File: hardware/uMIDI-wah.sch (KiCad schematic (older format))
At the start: 33 parts, among them IC1 Opamp_Dual_Generic, IC2 L78L09_SOT89, SW1 MMP221, X1 AudioJack3_Switch, X3 AudioJack3_Switch, X4 Conn_01x10

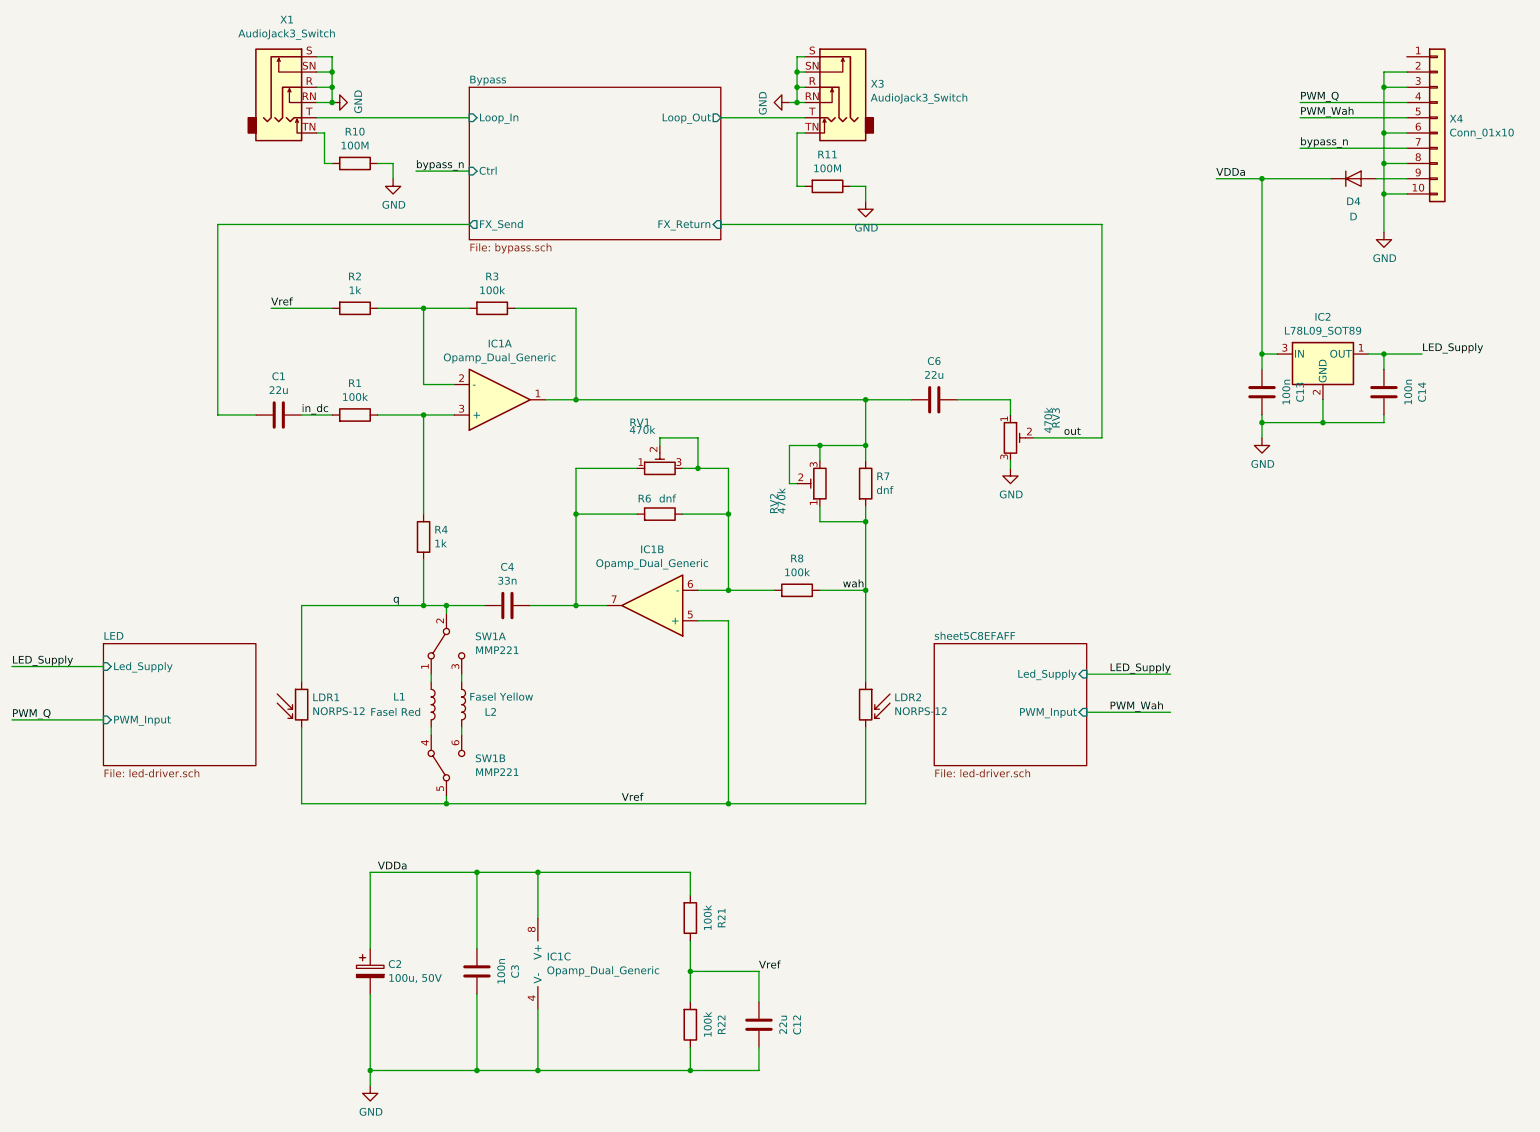
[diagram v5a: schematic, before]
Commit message: Use second relay to switch between inductors
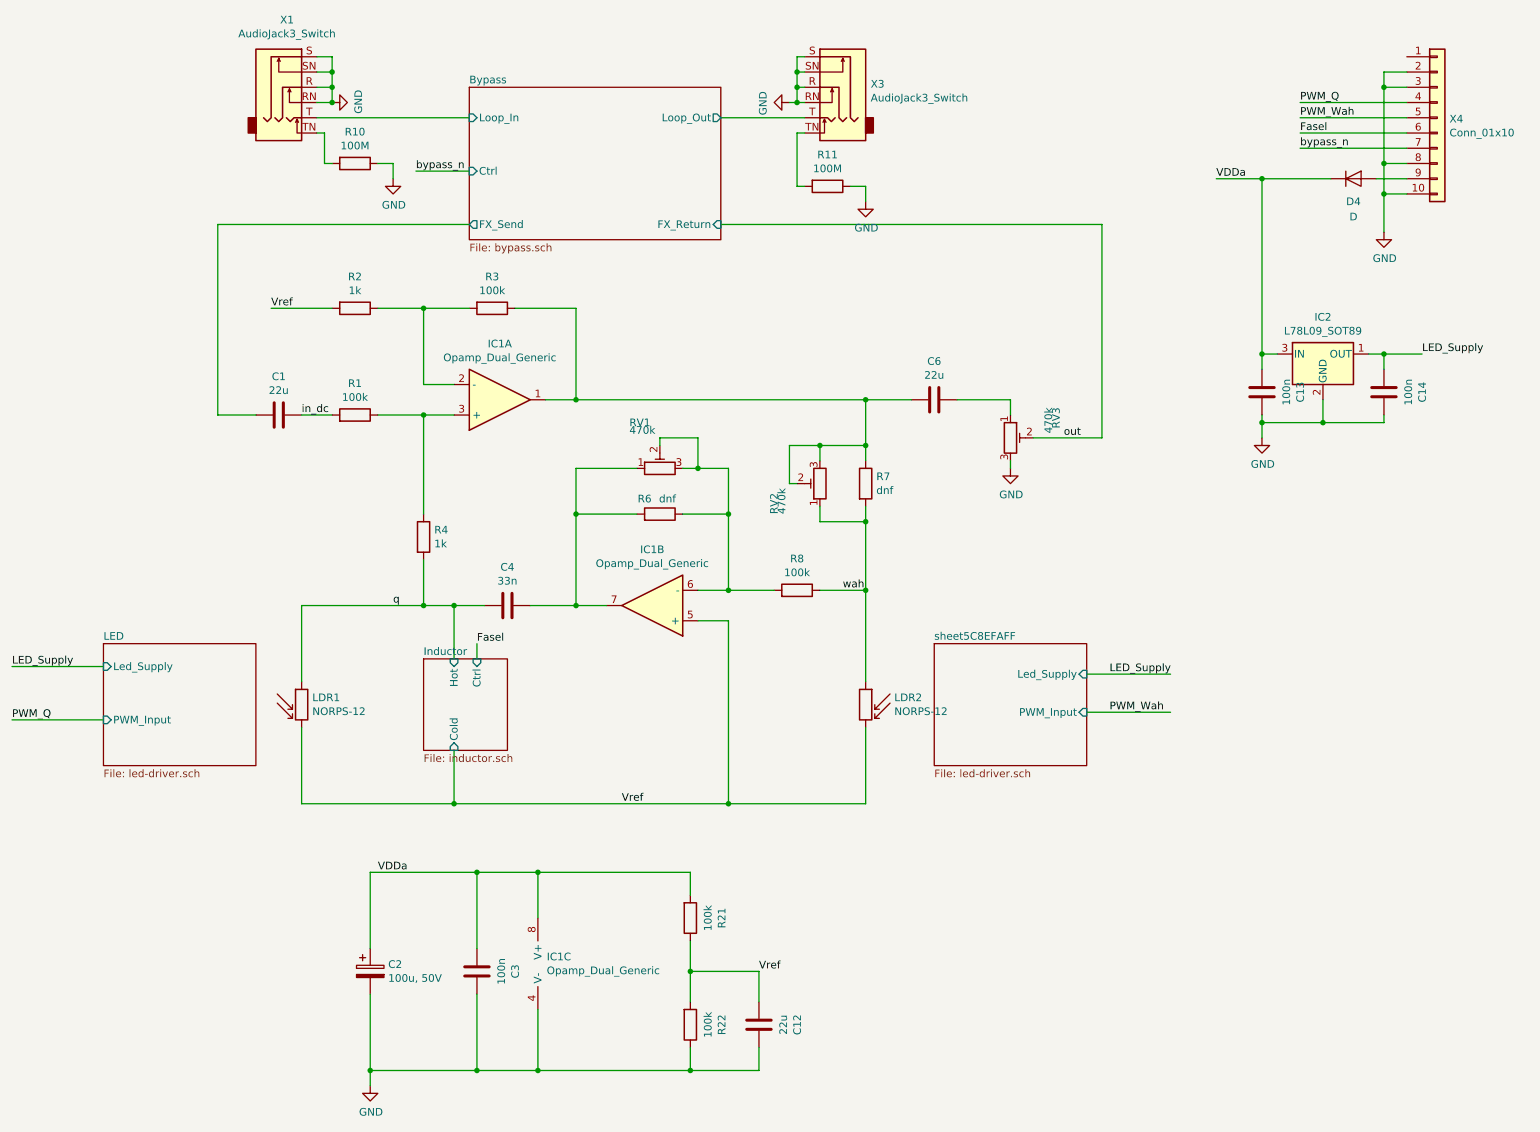
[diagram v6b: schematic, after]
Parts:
- removed L1: Fasel Red, umidi-wah:Fasel, symbol Device:L
- removed L2: Fasel Yellow, umidi-wah:Fasel, symbol Device:L
- removed SW1: MMP221, umidi-wah:MMP221, symbol Switch:SW_DPDT_x2
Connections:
- net GND: no longer X4.6 (Pin_6)
- new net Fasel: X4.6 (Pin_6)
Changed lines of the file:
@@
 $Descr A4 11693 8268
 encoding utf-8
-Sheet 1 4
+Sheet 1 5
 Title ""
 Date ""
@@
 	1    0    0    -1
 $EndComp
-$Comp
-L Device:L L1
-U 1 1 5C88342E
-P 3750 5000
-F 0 "L1" H 3500 5050 50  0000 L CNN
-F 1 "Fasel Red" H 3350 4950 50  0000 L CNN
-F 2 "umidi-wah:Fasel" H 3750 5000 50  0001 C CNN
-F 3 "~" H 3750 5000 50  0001 C CNN
-	1    3750 5000
-	1    0    0    -1
-$EndComp
 Wire Wire Line
 	5700 4250 5700 3750
@@
 Wire Wire Line
 	3700 4050 3700 4350
-Wire Wire Line
-	3700 4350 3850 4350
 Connection ~ 3700 4350
 Wire Wire Line
@@
 	10000 1900 10000 1650
 Wire Wire Line
-	10000 1250 10150 1250
-Wire Wire Line
 	10150 1650 10000 1650
 Connection ~ 10000 1650
@@
 Wire Wire Line
 	10150 1450 10000 1450
-Connection ~ 10000 1450
-Wire Wire Line
-	10000 1450 10000 1250
 Text Label 9450 1350 0    50   ~ 0
 bypass_n
@@
 	1    0    0    -1
 $EndComp
-$Comp
-L Switch:SW_DPDT_x2 SW1
-U 2 1 5CDB9DAE
-P 3850 5400
-F 0 "SW1" V 3896 5212 50  0000 R CNN
-F 1 "MMP221" V 3805 5212 50  0000 R CNN
-F 2 "umidi-wah:MMP221" H 3850 5400 50  0001 C CNN
-F 3 "https://docs-emea.rs-online.com/webdocs/0e2b/0900766b80e2b976.pdf" H 3850 5400 50  0001 C CNN
-F 4 "RS" V 3896 5212 50  0001 R CNN "Supplier"
-F 5 "745-5820" V 3896 5212 50  0001 R CNN "Supplier Part Number"
-F 6 "https://de.rs-online.com/web/p/schiebeschalter/7455820/" V 3896 5212 50  0001 R CNN "Supplier Link"
-F 7 "TE" V 3896 5212 50  0001 R CNN "Manufacturer"
-F 8 "1825163-1" V 3896 5212 50  0001 R CNN "Manufacturer Part Number"
-	2    3850 5400
-	0    -1   -1   0
-$EndComp
-$Comp
-L Switch:SW_DPDT_x2 SW1
-U 1 1 5CDBC60F
-P 3850 4600
-F 0 "SW1" V 3804 4412 50  0000 R CNN
-F 1 "MMP221" V 3895 4412 50  0000 R CNN
-F 2 "umidi-wah:MMP221" H 3850 4600 50  0001 C CNN
-F 3 "https://docs-emea.rs-online.com/webdocs/0e2b/0900766b80e2b976.pdf" H 3850 4600 50  0001 C CNN
-F 4 "RS" V 3804 4412 50  0001 R CNN "Supplier"
-F 5 "745-5820" V 3804 4412 50  0001 R CNN "Supplier Part Number"
-F 6 "https://de.rs-online.com/web/p/schiebeschalter/7455820/" V 3804 4412 50  0001 R CNN "Supplier Link"
-F 7 "TE" V 3804 4412 50  0001 R CNN "Manufacturer"
-F 8 "1825163-1" V 3804 4412 50  0001 R CNN "Manufacturer Part Number"
-	1    3850 4600
-	0    -1   1    0
-$EndComp
-Wire Wire Line
-	2900 5650 3850 5650
-$Comp
-L Device:L L2
-U 1 1 5CDFE763
-P 3950 5000
-F 0 "L2" H 4100 5050 50  0000 L CNN
-F 1 "Fasel Yellow" H 4000 4950 50  0000 L CNN
-F 2 "umidi-wah:Fasel" H 3950 5000 50  0001 C CNN
-F 3 "~" H 3950 5000 50  0001 C CNN
-	1    3950 5000
-	1    0    0    1
-$EndComp
-Wire Wire Line
-	3750 4800 3750 4850
-Wire Wire Line
-	3750 5150 3750 5200
-Wire Wire Line
-	3950 5200 3950 5150
-Wire Wire Line
-	3850 4400 3850 4350
-Connection ~ 3850 4350
-Wire Wire Line
-	3850 4350 4100 4350
-Wire Wire Line
-	3850 5600 3850 5650
-Connection ~ 3850 5650
-Wire Wire Line
-	3850 5650 5700 5650
-Wire Wire Line
-	3950 4850 3950 4800
 Wire Wire Line
 	3350 6100 4050 6100
@@
 Connection ~ 10000 2700
 Wire Wire Line
-	10000 1250 10000 950
-Wire Wire Line
 	10000 950  10150 950
-Connection ~ 10000 1250
 Wire Wire Line
 	9200 2700 9200 1550
@@
 	10150 850  10000 850
 Wire Wire Line
-	10000 850  10000 950
-Connection ~ 10000 950
-Wire Wire Line
 	4000 1500 3650 1500
 Text Label 3650 1500 0    50   ~ 0
 bypass_n
+$Sheet
+S 3700 4700 550  600
+U 5CE9535C
+F0 "Inductor" 50
+F1 "inductor.sch" 50
+F2 "Hot" I T 3900 4700 50
+F3 "Cold" I B 3900 5300 50
+F4 "Ctrl" I T 4050 4700 50
+$EndSheet
+Wire Wire Line
+	2900 5650 3900 5650
+Wire Wire Line
+	3700 4350 3900 4350
+Wire Wire Line
+	3900 4700 3900 4350
+Connection ~ 3900 4350
+Wire Wire Line
+	3900 4350 4100 4350
+Wire Wire Line
+	3900 5300 3900 5650
+Connection ~ 3900 5650
+Wire Wire Line
+	3900 5650 5700 5650
+Text Label 4050 4600 0    50   ~ 0
+Fasel
+Wire Wire Line
+	4050 4600 4050 4700
+Wire Wire Line
+	10000 850  10000 950
+Text Label 9450 1250 0    50   ~ 0
+Fasel
+Wire Wire Line
+	9450 1250 10150 1250
+Wire Wire Line
+	10000 1450 10000 950
+Connection ~ 10000 1450
+Connection ~ 10000 950
 $EndSCHEMATC

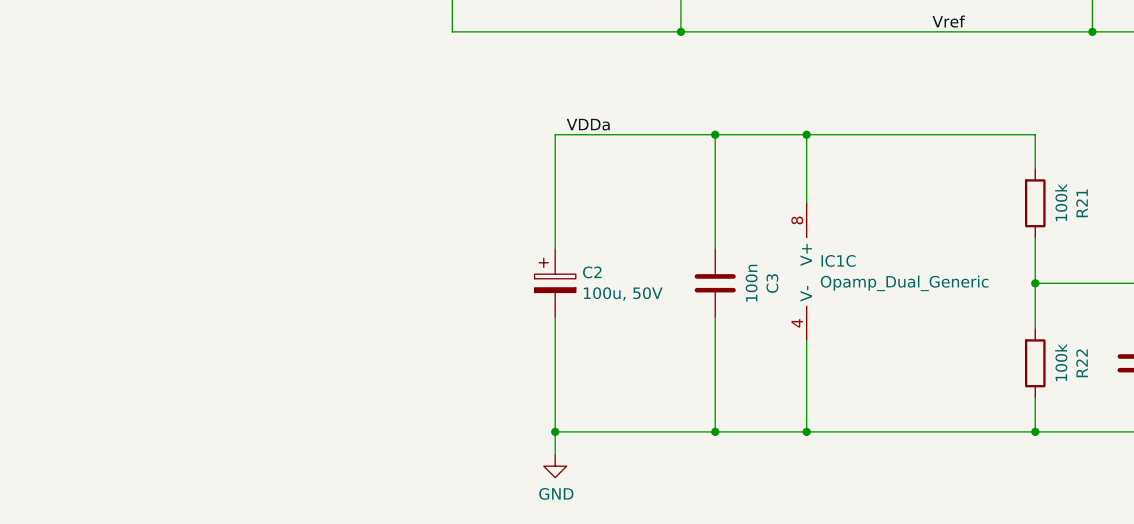
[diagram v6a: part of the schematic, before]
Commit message: Add missing manufacturer links
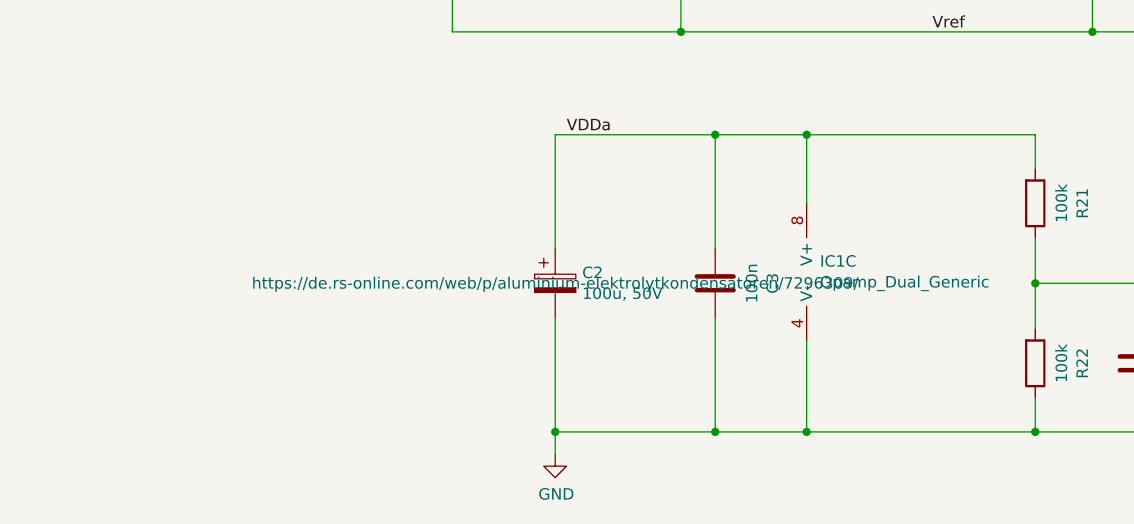
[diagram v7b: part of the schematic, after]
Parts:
- C1, C12, C6: Supplier (none) -> RS; Supplier Link (none) -> https://de.rs-online.com/web/p/keramik-vielschichtkondensat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; Supplier Part Number (none) -> 169-2721
- C13, C14, C3: Supplier (none) -> RS; Supplier Link (none) -> https://de.rs-online.com/web/p/keramik-vielschichtkondensat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; Supplier Part Number (none) -> 170-0041
- C2: Supplier Link (none) -> https://de.rs-online.com/web/p/aluminium-elektrolytkondensa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
- C4: Supplier (none) -> RS; Supplier Link (none) -> https://de.rs-online.com/web/p/keramik-vielschichtkondensat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; Supplier Part Number (none) -> 169-6231
- R1, R21, R22, R3, R8: Supplier (none) -> RS; Supplier Link (none) -> https://de.rs-online.com/web/p/smd-widerstande/8046607/; Supplier Part Number (none) -> 804-6607
- R10, R11: Supplier (none) -> RS; Supplier Link (none) -> https://de.rs-online.com/web/p/smd-widerstande/2945062/; Supplier Part Number (none) -> 294-5062
- R2, R4: Supplier (none) -> RS; Supplier Link (none) -> https://de.rs-online.com/web/p/smd-widerstande/8046449/; Supplier Part Number (none) -> 804-6449
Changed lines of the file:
@@
 EESchema Schematic File Version 4
-LIBS:uMIDI-wah-cache
-EELAYER 29 0
+EELAYER 30 0
 EELAYER END
 $Descr A4 11693 8268
@@
 F 2 "Resistor_SMD:R_0805_2012Metric_Pad1.15x1.40mm_HandSolder" V 3180 2400 50  0001 C CNN
 F 3 "" H 3250 2400 50  0001 C CNN
+F 4 "RS" V 3043 2400 50  0001 C CNN "Supplier"
+F 5 "804-6449" V 3043 2400 50  0001 C CNN "Supplier Part Number"
+F 6 "https://de.rs-online.com/web/p/smd-widerstande/8046449/" V 3043 2400 50  0001 C CNN "Supplier Link"
 	1    3250 2400
 	0    1    1    0
@@
 F 2 "Resistor_SMD:R_0805_2012Metric_Pad1.15x1.40mm_HandSolder" V 3180 3100 50  0001 C CNN
 F 3 "" H 3250 3100 50  0001 C CNN
+F 4 "RS" V 3457 3100 50  0001 C CNN "Supplier"
+F 5 "804-6607" V 3457 3100 50  0001 C CNN "Supplier Part Number"
+F 6 "https://de.rs-online.com/web/p/smd-widerstande/8046607/" V 3457 3100 50  0001 C CNN "Supplier Link"
 	1    3250 3100
 	0    1    -1   0
@@
 F 2 "Resistor_SMD:R_0805_2012Metric_Pad1.15x1.40mm_HandSolder" V 3630 3900 50  0001 C CNN
 F 3 "" H 3700 3900 50  0001 C CNN
+F 4 "RS" H 3770 3946 50  0001 L CNN "Supplier"
+F 5 "804-6449" H 3770 3946 50  0001 L CNN "Supplier Part Number"
+F 6 "https://de.rs-online.com/web/p/smd-widerstande/8046449/" H 3770 3946 50  0001 L CNN "Supplier Link"
 	1    3700 3900
 	1    0    0    -1
@@
 F 2 "Resistor_SMD:R_0805_2012Metric_Pad1.15x1.40mm_HandSolder" V 6080 4250 50  0001 C CNN
 F 3 "" H 6150 4250 50  0001 C CNN
+F 4 "RS" V 6357 4250 50  0001 C CNN "Supplier"
+F 5 "804-6607" V 6357 4250 50  0001 C CNN "Supplier Part Number"
+F 6 "https://de.rs-online.com/web/p/smd-widerstande/8046607/" V 6357 4250 50  0001 C CNN "Supplier Link"
 	1    6150 4250
 	0    1    -1   0
@@
 F 2 "Resistor_SMD:R_0805_2012Metric_Pad1.15x1.40mm_HandSolder" V 4080 2400 50  0001 C CNN
 F 3 "" H 4150 2400 50  0001 C CNN
+F 4 "RS" V 3943 2400 50  0001 C CNN "Supplier"
+F 5 "804-6607" V 3943 2400 50  0001 C CNN "Supplier Part Number"
+F 6 "https://de.rs-online.com/web/p/smd-widerstande/8046607/" V 3943 2400 50  0001 C CNN "Supplier Link"
 	1    4150 2400
 	0    1    1    0
@@
 F 2 "Capacitor_SMD:C_0805_2012Metric_Pad1.15x1.40mm_HandSolder" H 7088 2850 50  0001 C CNN
 F 3 "" H 7050 3000 50  0001 C CNN
+F 4 "RS" V 6798 3000 50  0001 C CNN "Supplier"
+F 5 "169-2721" V 6798 3000 50  0001 C CNN "Supplier Part Number"
+F 6 "https://de.rs-online.com/web/p/keramik-vielschichtkondensatoren/1692721/" V 6798 3000 50  0001 C CNN "Supplier Link"
 	1    7050 3000
 	0    1    1    0
@@
 F 2 "Capacitor_SMD:C_0805_2012Metric_Pad1.15x1.40mm_HandSolder" H 4288 4200 50  0001 C CNN
 F 3 "" H 4250 4350 50  0001 C CNN
+F 4 "RS" V 3998 4350 50  0001 C CNN "Supplier"
+F 5 "169-6231" V 3998 4350 50  0001 C CNN "Supplier Part Number"
+F 6 "https://de.rs-online.com/web/p/keramik-vielschichtkondensatoren/1696231/" V 3998 4350 50  0001 C CNN "Supplier Link"
 	1    4250 4350
 	0    1    1    0
@@
 F 2 "Capacitor_SMD:C_0805_2012Metric_Pad1.15x1.40mm_HandSolder" H 2788 2950 50  0001 C CNN
 F 3 "" H 2750 3100 50  0001 C CNN
+F 4 "RS" V 2498 3100 50  0001 C CNN "Supplier"
+F 5 "169-2721" V 2498 3100 50  0001 C CNN "Supplier Part Number"
+F 6 "https://de.rs-online.com/web/p/keramik-vielschichtkondensatoren/1692721/" V 2498 3100 50  0001 C CNN "Supplier Link"
 	1    2750 3100
 	0    1    1    0
@@
 F 2 "Resistor_SMD:R_0805_2012Metric_Pad1.15x1.40mm_HandSolder" V 3180 1450 50  0001 C CNN
 F 3 "" H 3250 1450 50  0001 C CNN
+F 4 "RS" V 3043 1450 50  0001 C CNN "Supplier"
+F 5 "294-5062" V 3043 1450 50  0001 C CNN "Supplier Part Number"
+F 6 "https://de.rs-online.com/web/p/smd-widerstande/2945062/" V 3043 1450 50  0001 C CNN "Supplier Link"
+F 7 "" V 3043 1450 50  0001 C CNN "Manufacturer"
+F 8 "" V 3043 1450 50  0001 C CNN "Manufacturer Part Number"
 	1    3250 1450
 	0    1    1    0
@@
 F 2 "Resistor_SMD:R_0805_2012Metric_Pad1.15x1.40mm_HandSolder" V 6280 1600 50  0001 C CNN
 F 3 "" H 6350 1600 50  0001 C CNN
+F 4 "RS" V 6143 1600 50  0001 C CNN "Supplier"
+F 5 "294-5062" V 6143 1600 50  0001 C CNN "Supplier Part Number"
+F 6 "https://de.rs-online.com/web/p/smd-widerstande/2945062/" V 6143 1600 50  0001 C CNN "Supplier Link"
+F 7 "" V 6143 1600 50  0001 C CNN "Manufacturer"
+F 8 "" V 6143 1600 50  0001 C CNN "Manufacturer Part Number"
 	1    6350 1600
 	0    1    1    0
@@
 F 2 "Capacitor_SMD:C_0805_2012Metric_Pad1.15x1.40mm_HandSolder" H 4088 6600 50  0001 C CNN
 F 3 "" H 4050 6750 50  0001 C CNN
+F 4 "RS" V 3798 6750 50  0001 C CNN "Supplier"
+F 5 "170-0041" V 3798 6750 50  0001 C CNN "Supplier Part Number"
+F 6 "https://de.rs-online.com/web/p/keramik-vielschichtkondensatoren/1700041/" V 3798 6750 50  0001 C CNN "Supplier Link"
+F 7 "" V 3798 6750 50  0001 C CNN "Manufacturer"
+F 8 "" V 3798 6750 50  0001 C CNN "Manufacturer Part Number"
 	1    4050 6750
 	-1   0    0    1
@@
 F 2 "Resistor_SMD:R_0805_2012Metric_Pad1.15x1.40mm_HandSolder" V 5380 6400 50  0001 C CNN
 F 3 "" H 5450 6400 50  0001 C CNN
+F 4 "RS" V 5657 6400 50  0001 C CNN "Supplier"
+F 5 "804-6607" V 5657 6400 50  0001 C CNN "Supplier Part Number"
+F 6 "https://de.rs-online.com/web/p/smd-widerstande/8046607/" V 5657 6400 50  0001 C CNN "Supplier Link"
 	1    5450 6400
 	1    0    0    1
@@
 F 2 "Resistor_SMD:R_0805_2012Metric_Pad1.15x1.40mm_HandSolder" V 5380 7100 50  0001 C CNN
 F 3 "" H 5450 7100 50  0001 C CNN
+F 4 "RS" V 5657 7100 50  0001 C CNN "Supplier"
+F 5 "804-6607" V 5657 7100 50  0001 C CNN "Supplier Part Number"
+F 6 "https://de.rs-online.com/web/p/smd-widerstande/8046607/" V 5657 7100 50  0001 C CNN "Supplier Link"
 	1    5450 7100
 	1    0    0    1
@@
 F 4 "RS" H 3350 6750 50  0001 C CNN "Supplier"
 F 5 " 729-6309" H 3350 6750 50  0001 C CNN "Supplier Part Number"
+F 6 "https://de.rs-online.com/web/p/aluminium-elektrolytkondensatoren/7296309/" H 3350 6750 50  0000 C CNN "Supplier Link"
 	1    3350 6750
 	1    0    0    -1
@@
 F 2 "Capacitor_SMD:C_0805_2012Metric_Pad1.15x1.40mm_HandSolder" H 5938 6950 50  0001 C CNN
 F 3 "" H 5900 7100 50  0001 C CNN
+F 4 "RS" V 5648 7100 50  0001 C CNN "Supplier"
+F 5 "169-2721" V 5648 7100 50  0001 C CNN "Supplier Part Number"
+F 6 "https://de.rs-online.com/web/p/keramik-vielschichtkondensatoren/1692721/" V 5648 7100 50  0001 C CNN "Supplier Link"
 	1    5900 7100
 	-1   0    0    1
@@
 F 2 "Capacitor_SMD:C_0805_2012Metric_Pad1.15x1.40mm_HandSolder" H 10038 2800 50  0001 C CNN
 F 3 "" H 10000 2950 50  0001 C CNN
+F 4 "RS" V 9748 2950 50  0001 C CNN "Supplier"
+F 5 "170-0041" V 9748 2950 50  0001 C CNN "Supplier Part Number"
+F 6 "https://de.rs-online.com/web/p/keramik-vielschichtkondensatoren/1700041/" V 9748 2950 50  0001 C CNN "Supplier Link"
+F 7 "" V 9748 2950 50  0001 C CNN "Manufacturer"
+F 8 "" V 9748 2950 50  0001 C CNN "Manufacturer Part Number"
 	1    10000 2950
 	-1   0    0    1
@@
 F 2 "Capacitor_SMD:C_0805_2012Metric_Pad1.15x1.40mm_HandSolder" H 9238 2800 50  0001 C CNN
 F 3 "" H 9200 2950 50  0001 C CNN
+F 4 "RS" V 8948 2950 50  0001 C CNN "Supplier"
+F 5 "170-0041" V 8948 2950 50  0001 C CNN "Supplier Part Number"
+F 6 "https://de.rs-online.com/web/p/keramik-vielschichtkondensatoren/1700041/" V 8948 2950 50  0001 C CNN "Supplier Link"
+F 7 "" V 8948 2950 50  0001 C CNN "Manufacturer"
+F 8 "" V 8948 2950 50  0001 C CNN "Manufacturer Part Number"
 	1    9200 2950
 	-1   0    0    1
